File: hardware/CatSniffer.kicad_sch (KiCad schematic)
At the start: 90 parts, among them J1 Antenna, J3 Conn_01x06_Female, P1 USB_C_Plug_USB2.0, SW1 SW, U1 AP2112K-3.3, U2 RFSW8006QTR7, U3 RP2040, U4 0900PC15A0036, U5 0900FM15D0039, U6 PE42421, U7 SX1262IMLTRT, U8 CC1352P74T0RGZR, U9 W25Q16JV, Y1 48MHz, Y2 32.768kHz, Y3 32Mhz, Y4 12MHz

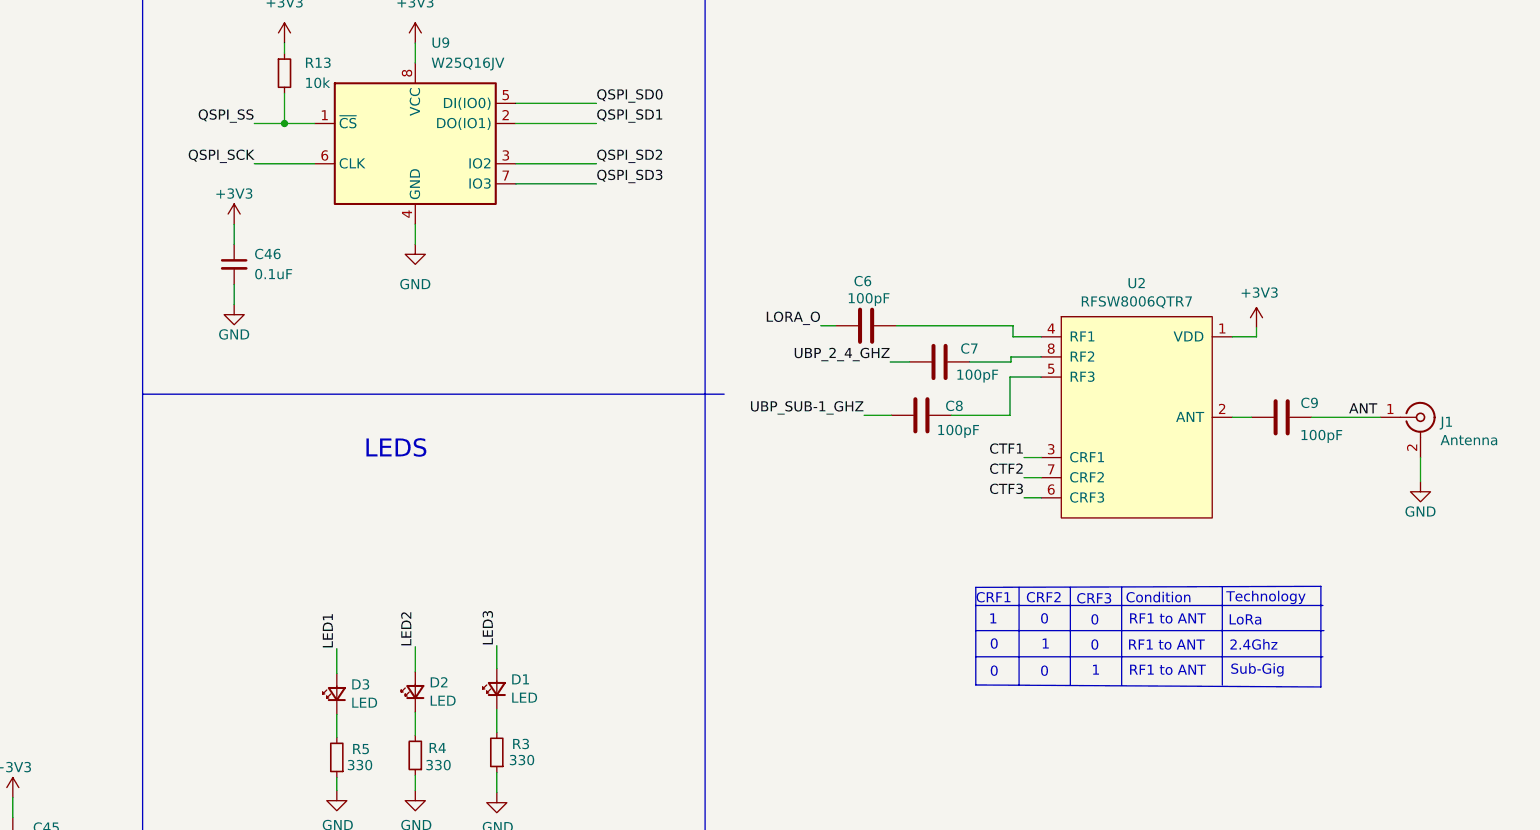
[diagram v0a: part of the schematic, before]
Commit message: Feat(Hw):Changed_antenna_switch
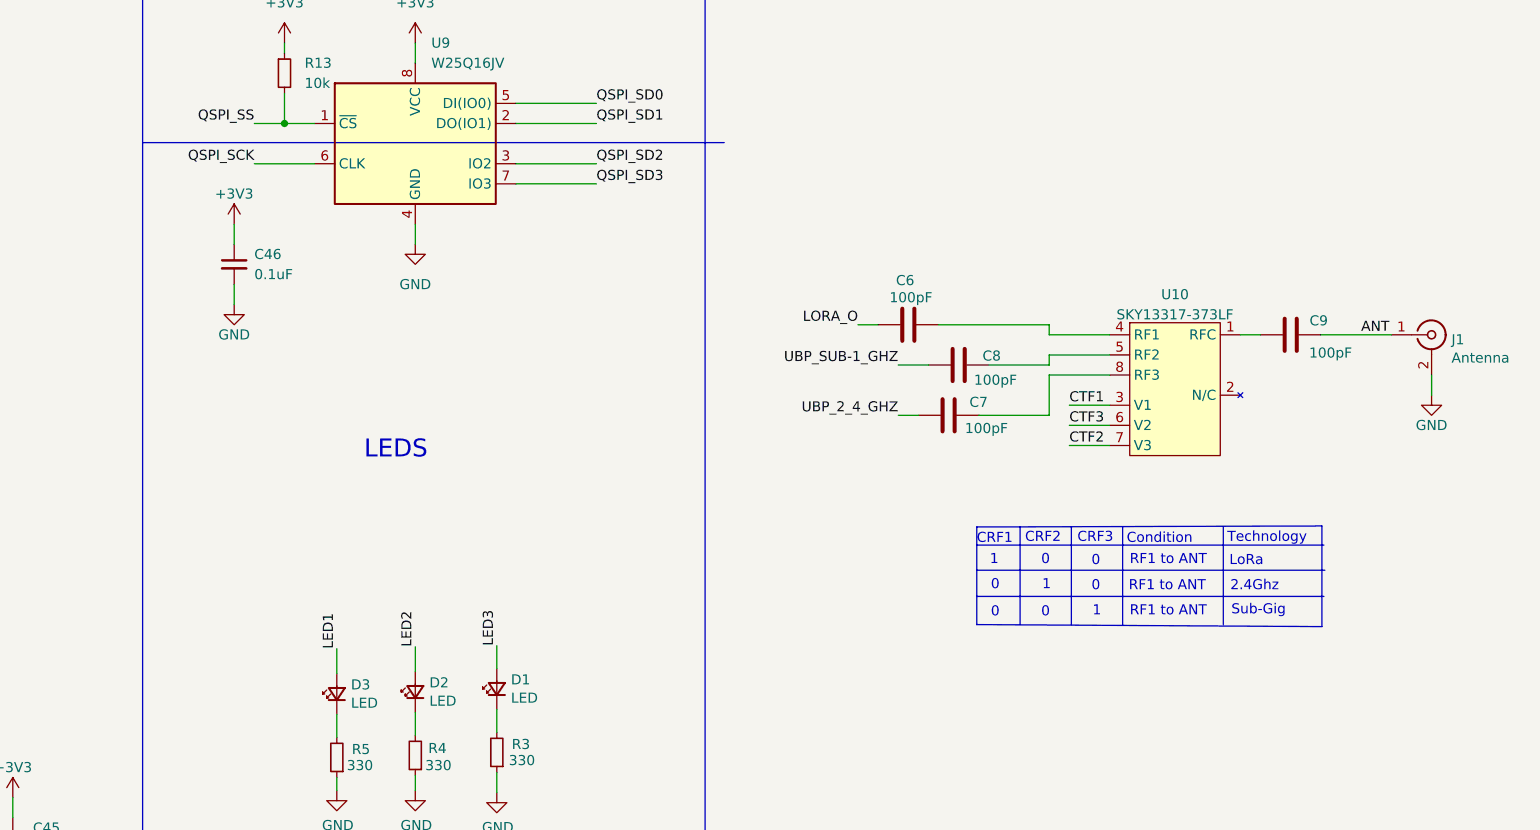
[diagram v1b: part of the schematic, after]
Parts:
- removed U2: RFSW8006QTR7, CatSniffer:SON50P200X200X90-9N, symbol CatSniffer-rescue:RFSW8006QTR7-electroniccats-CatStick-rescue-CatSniffer-rescue
- added U10: SKY13317-373LF, symbol Radio:SKY13317-373LF
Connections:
- net CTF1: now also U10.3 (V1)
- net CTF2: now also U10.7 (V3)
- net CTF3: now also U10.6 (V2)
- net at C9.1: now also U10.1 (RFC)
- net at C6.2: now also U10.4 (RF1)
- net at C8.2: now also U10.5 (RF2)
- net at C7.2: now also U10.8 (RF3)
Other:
- moved on the sheet: C6, C7, C8, C9, J1

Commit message: fix(Hw):fixed_switch_text
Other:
- note added: "CTF1"
- note added: "CTF2"
- note added: "CTF3"
- note removed: "CRF1"
- note removed: "CRF2"
- note removed: "CRF3"
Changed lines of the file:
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@@
 		)
 	)
-	(text "CRF2"
+	(text "CTF2"
 		(exclude_from_sim no)
 		(at 518.922 93.726 0)
@@
 		)
 	)
-	(text "CRF1"
+	(text "CTF1"
 		(exclude_from_sim no)
 		(at 512.826 93.853 0)
@@
 		)
 	)
-	(text "CRF3"
+	(text "CTF3"
 		(exclude_from_sim no)
 		(at 525.526 93.726 0)
@@
 	(polyline
 		(pts
-			(xy 407.543 43.053) (xy 480.949 43.053)
-		)
-		(stroke
+			(xy 407.67 74.295) (xy 478.79 74.295)
+		)
+		(stroke

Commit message: Feat(Hw):changed_switch_capacitors_to_47uf
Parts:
- C6, C7, C8: value 100pF -> 47pF; LCSC# C14858 -> C519486
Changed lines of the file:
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@@
 			)
 		)
-		(property "Value" "100pF"
+		(property "Value" "47pF"
 			(at 507.238 62.611 90)
 			(effects
@@
 			)
 		)
-		(property "LCSC#" "C14858"
+		(property "LCSC#" "C519486"
 			(at 504.19 66.04 0)
 			(effects
@@
 			)
 		)
-		(property "Value" "100pF"
+		(property "Value" "47pF"
 			(at 516.763 79.121 90)
 			(effects
@@
 			)
 		)
-		(property "LCSC#" "C14858"
+		(property "LCSC#" "C519486"
 			(at 509.27 77.47 0)
 			(effects
@@
 			)
 		)
-		(property "Value" "100pF"
+		(property "Value" "47pF"
 			(at 517.906 73.025 90)
 			(effects
@@
 			)
 		)
-		(property "LCSC#" "C14858"
-			(at 510.54 71.12 0)
-			(effects
+		(property "LCSC#" "C519486"
+			(at 510.54 71.12 0)
+			(effects
